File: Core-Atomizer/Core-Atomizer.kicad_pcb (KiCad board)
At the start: 2 copper layers, 23 x 14 mm, 16 parts, among them J1 PH-4AW, J2 PH-2AW环保, Q1 CJ2102, Q2 CJ2102, U1 NL17SZ14DFT2G

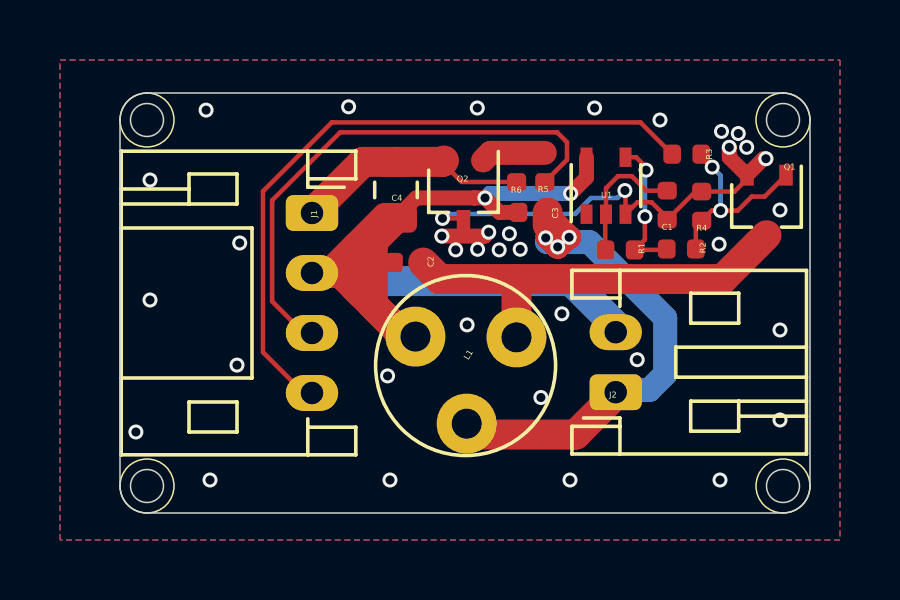
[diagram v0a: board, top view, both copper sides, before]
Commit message: 订正inductor封装，增加丝印
Signed-off-by: fuhua-chen <fuhua-chen@outlook.com>
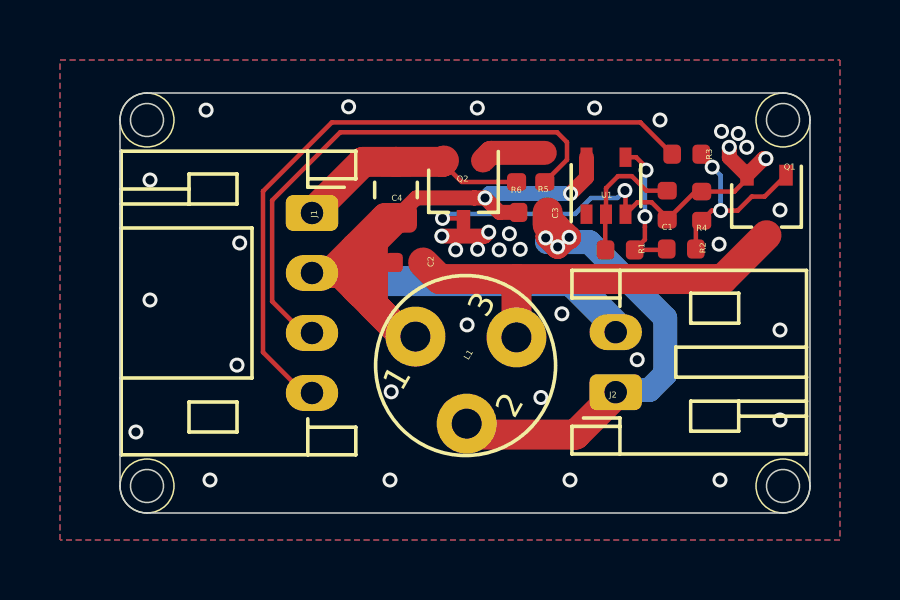
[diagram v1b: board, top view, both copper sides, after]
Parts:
- L1: footprint Inductor_3Pins_6x8mm -> Pinno:Inductor_3Pins_6x8mm
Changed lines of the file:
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@@
   (page A4)
   (layers
-    (0 F.Cu signal hide)
-    (31 B.Cu signal hide)
-    (32 B.Adhes user hide)
-    (33 F.Adhes user hide)
-    (34 B.Paste user hide)
-    (35 F.Paste user hide)
+    (0 F.Cu signal)
+    (31 B.Cu signal)
+    (32 B.Adhes user)
+    (33 F.Adhes user)
+    (34 B.Paste user)
+    (35 F.Paste user)
     (36 B.SilkS user)
     (37 F.SilkS user)
-    (38 B.Mask user hide)
-    (39 F.Mask user hide)
+    (38 B.Mask user)
+    (39 F.Mask user)
     (40 Dwgs.User user)
     (41 Cmts.User user)
@@
   )
   (setup
-    (last_trace_width 0.5)
+    (last_trace_width 0.152)
     (user_trace_width 0.254)
     (user_trace_width 0.5)
@@
     (pad_to_mask_clearance 0)
     (aux_axis_origin 0 0)
-    (visible_elements FFFFFF7F)
+    (visible_elements 7FFFFFFF)
     (pcbplotparams
       (layerselection 0x010fc_ffffffff)
-      (usegerberextensions false)
+      (usegerberextensions true)
       (usegerberattributes false)
       (usegerberadvancedattributes false)
-      (creategerberjobfile false)
+      (creategerberjobfile true)
       (excludeedgelayer true)
-      (linewidth 0.100000)
+      (linewidth 0.020000)
       (plotframeref false)
       (viasonmask false)
@@
       (psnegative false)
       (psa4output false)
-      (plotreference true)
-      (plotvalue true)
+      (plotreference false)
+      (plotvalue false)
       (plotinvisibletext false)
-      (padsonsilk false)
+      (padsonsilk true)
       (subtractmaskfromsilk false)
       (outputformat 1)
       (mirror false)
-      (drillshape 1)
+      (drillshape 0)
       (scaleselection 1)
-      (outputdirectory ""))
+      (outputdirectory "Core-Atomizer v0.1-Gerber"))
   )
   (net 0 "")
@@
     (add_net "Net-(Q2-Pad1)")
     (add_net "Net-(R1-Pad2)")
-    (add_net "Net-(U1-Pad1)")
+  )
+  (module Pinno:Inductor_3Pins_6x8mm (layer F.Cu)
+    (at 123.52 75.184 60)
+    (fp_text reference L1 (at 0.36 -0.1 60) (layer F.SilkS)
+      (effects (font (size 0.2 0.2) (thickness 0.05)))
+    )
+    (fp_text value IND_3Pins_22uH_720uH_6x8mm (at -0.004049 -0.575013 60) (layer F.Fab)
+      (effects (font (size 0.2 0.2) (thickness 0.05)))
+    )
+    (fp_text user 3 (at 2.04 -0.55 60) (layer F.SilkS)
+      (effects (font (size 0.8 0.8) (thickness 0.15)))
+    )
+    (fp_text user 2 (at -0.4 1.93 60) (layer F.SilkS)
+      (effects (font (size 0.8 0.8) (thickness 0.15)))
+    )
+    (fp_text user 1 (at -1.5 -1.77 60) (layer F.SilkS)
+      (effects (font (size 0.8 0.8) (thickness 0.15)))
+    )
+    (fp_text user %R (at 0.36 -0.1 60) (layer F.Fab)
+      (effects (font (size 0.2 0.2) (thickness 0.05)))
+    )
+    (fp_circle (center 0 0) (end 3 0) (layer F.SilkS) (width 0.12))
+    (pad 3 thru_hole circle (at 1.66 1 60) (size 2 2) (drill 1) (layers *.Cu *.Mask)
+      (net 2 "Net-(C2-Pad2)"))
+    (pad 2 thru_hole circle (at -1.66 1 60) (size 2 2) (drill 1) (layers *.Cu *.Mask)
+      (net 4 "Net-(C3-Pad2)"))
+    (pad 1 thru_hole circle (at 0 -1.93 60) (size 2 2) (drill 1) (layers *.Cu *.Mask)
+      (net 3 /VCC))
   )
   (module R_0402_1005Metric (layer F.Cu)
@@
     )
   )
-  (module Inductor_3Pins_6x8mm (layer F.Cu)
-    (at 123.52 75.184 60)
-    (fp_text reference L1 (at 0.36 -0.1 60) (layer F.SilkS)
-      (effects (font (size 0.2 0.2) (thickness 0.05)))
-    )
-    (fp_text value IND_3Pins_22uH_720uH_6x8mm (at -0.004049 -0.575013 60) (layer F.Fab)
-      (effects (font (size 0.2 0.2) (thickness 0.05)))
-    )
-    (fp_circle (center 0 0) (end 3 0) (layer F.SilkS) (width 0.12))
-    (fp_text user %R (at 0.36 -0.1 60) (layer F.Fab)
-      (effects (font (size 0.2 0.2) (thickness 0.05)))
-    )
-    (pad 1 thru_hole circle (at 0 -1.93 60) (size 2 2) (drill 1) (layers *.Cu *.Mask)
-      (net 3 /VCC))
-    (pad 2 thru_hole circle (at -1.66 1 60) (size 2 2) (drill 1) (layers *.Cu *.Mask)
-      (net 4 "Net-(C3-Pad2)"))
-    (pad 3 thru_hole circle (at 1.66 1 60) (size 2 2) (drill 1) (layers *.Cu *.Mask)
-      (net 2 "Net-(C2-Pad2)"))
-  )
   (module SOT-323_SC-70 (layer F.Cu)
     (at 133.55 69.84 270)
@@
   (segment (start 129.542444 69.355) (end 129.059442 68.871998) (width 0.152) (layer F.Cu) (net 1))
   (segment (start 130.24 69.355) (end 129.542444 69.355) (width 0.152) (layer F.Cu) (net 1))
-  (segment (start 131.18 69.385) (end 131.39 69.385) (width 0.152) (layer F.Cu) (net 11))
-  (segment (start 130.24 70.325) (end 131.18 69.385) (width 0.152) (layer F.Cu) (net 11))
-  (segment (start 129.719441 69.741999) (end 129.248001 69.741999) (width 0.152) (layer F.Cu) (net 11))
-  (segment (start 130.24 70.325) (end 130.24 70.262558) (width 0.152) (layer F.Cu) (net 11))
-  (segment (start 130.24 70.262558) (end 129.719441 69.741999) (width 0.152) (layer F.Cu) (net 11))
-  (segment (start 129.248001 69.741999) (end 128.85 70.14) (width 0.152) (layer F.Cu) (net 11))
-  (via (at 128.83 69.35) (size 0.5) (drill 0.3) (layers F.Cu B.Cu) (net 11))
-  (segment (start 128.85 69.37) (end 128.83 69.35) (width 0.152) (layer F.Cu) (net 11))
-  (segment (start 128.85 70.14) (end 128.85 69.37) (width 0.152) (layer F.Cu) (net 11))
-  (segment (start 128.580001 69.599999) (end 127.700001 69.599999) (width 0.152) (layer B.Cu) (net 11))
-  (segment (start 128.83 69.35) (end 128.580001 69.599999) (width 0.152) (layer B.Cu) (net 11))
-  (segment (start 127.700001 69.599999) (end 127.17 70.13) (width 0.152) (layer B.Cu) (net 11))
-  (via (at 122.75 70.28) (size 0.5) (drill 0.3) (layers F.Cu B.Cu) (net 11))
-  (segment (start 127.17 70.13) (end 122.9 70.13) (width 0.152) (layer B.Cu) (net 11))
-  (segment (start 122.9 70.13) (end 122.75 70.28) (width 0.152) (layer B.Cu) (net 11))
-  (segment (start 123.38 70.28) (end 123.45 70.35) (width 0.152) (layer F.Cu) (net 11))
-  (segment (start 122.75 70.28) (end 123.38 70.28) (width 0.152) (layer F.Cu) (net 11))
-  (segment (start 132.9 68.965) (end 132.9 68.84) (width 0.152) (layer F.Cu) (net 11))
-  (segment (start 132.48 69.385) (end 132.9 68.965) (width 0.152) (layer F.Cu) (net 11))
-  (segment (start 131.39 69.385) (end 132.48 69.385) (width 0.152) (layer F.Cu) (net 11))
-  (segment (start 131.36 70.325) (end 131.39 70.355) (width 0.152) (layer F.Cu) (net 8))
   (segment (start 122.105 71.75) (end 122.65701 72.30201) (width 1) (layer F.Cu) (net 2))
   (segment (start 125.216025 72.317995) (end 125.216025 74.612398) (width 1) (layer F.Cu) (net 2))
@@
   (segment (start 116.76599 69.37401) (end 116.76599 74.74099) (width 0.152) (layer F.Cu) (net 7))
   (segment (start 118.125 76.1) (end 118.4 76.1) (width 0.152) (layer F.Cu) (net 7))
+  (segment (start 131.36 70.325) (end 131.39 70.355) (width 0.152) (layer F.Cu) (net 8))
   (segment (start 131.195 70.55) (end 131.39 70.355) (width 0.152) (layer F.Cu) (net 8))
   (segment (start 131.195 71.3) (end 131.195 70.55) (width 0.152) (layer F.Cu) (net 8))
@@
   (segment (start 129.496977 70.988023) (end 129.496977 70.574425) (width 0.152) (layer F.Cu) (net 10))
   (segment (start 129.155 71.33) (end 129.496977 70.988023) (width 0.152) (layer F.Cu) (net 10))
+  (segment (start 131.18 69.385) (end 131.39 69.385) (width 0.152) (layer F.Cu) (net 11))
+  (segment (start 130.24 70.325) (end 131.18 69.385) (width 0.152) (layer F.Cu) (net 11))
+  (segment (start 129.719441 69.741999) (end 129.248001 69.741999) (width 0.152) (layer F.Cu) (net 11))
+  (segment (start 130.24 70.325) (end 130.24 70.262558) (width 0.152) (layer F.Cu) (net 11))
+  (segment (start 130.24 70.262558) (end 129.719441 69.741999) (width 0.152) (layer F.Cu) (net 11))
+  (segment (start 129.248001 69.741999) (end 128.85 70.14) (width 0.152) (layer F.Cu) (net 11))
+  (via (at 128.83 69.35) (size 0.5) (drill 0.3) (layers F.Cu B.Cu) (net 11))
+  (segment (start 128.85 69.37) (end 128.83 69.35) (width 0.152) (layer F.Cu) (net 11))
+  (segment (start 128.85 70.14) (end 128.85 69.37) (width 0.152) (layer F.Cu) (net 11))
+  (segment (start 128.580001 69.599999) (end 127.700001 69.599999) (width 0.152) (layer B.Cu) (net 11))
+  (segment (start 128.83 69.35) (end 128.580001 69.599999) (width 0.152) (layer B.Cu) (net 11))
+  (segment (start 127.700001 69.599999) (end 127.17 70.13) (width 0.152) (layer B.Cu) (net 11))
+  (via (at 122.75 70.28) (size 0.5) (drill 0.3) (layers F.Cu B.Cu) (net 11))
+  (segment (start 127.17 70.13) (end 122.9 70.13) (width 0.152) (layer B.Cu) (net 11))
+  (segment (start 122.9 70.13) (end 122.75 70.28) (width 0.152) (layer B.Cu) (net 11))
+  (segment (start 123.38 70.28) (end 123.45 70.35) (width 0.152) (layer F.Cu) (net 11))
+  (segment (start 122.75 70.28) (end 123.38 70.28) (width 0.152) (layer F.Cu) (net 11))
+  (segment (start 132.9 68.965) (end 132.9 68.84) (width 0.152) (layer F.Cu) (net 11))
+  (segment (start 132.48 69.385) (end 132.9 68.965) (width 0.152) (layer F.Cu) (net 11))
+  (segment (start 131.39 69.385) (end 132.48 69.385) (width 0.152) (layer F.Cu) (net 11))
   (via (at 112.53 77.4) (size 0.5) (drill 0.3) (layers F.Cu B.Cu) (net 11))
   (via (at 113 73) (size 0.5) (drill 0.3) (layers F.Cu B.Cu) (net 11))
@@
   (via (at 115.99 71.1) (size 0.5) (drill 0.3) (layers F.Cu B.Cu) (net 11))
   (via (at 115.9 75.17) (size 0.5) (drill 0.3) (layers F.Cu B.Cu) (net 11))
-  (via (at 120.92 75.53) (size 0.5) (drill 0.3) (layers F.Cu B.Cu) (net 11))
+  (via (at 121.04 76.06) (size 0.5) (drill 0.3) (layers F.Cu B.Cu) (net 11))
   (via (at 123.57 73.83) (size 0.5) (drill 0.3) (layers F.Cu B.Cu) (net 11))
   (via (at 122.73 70.87) (size 0.5) (drill 0.3) (layers F.Cu B.Cu) (net 11))

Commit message: 更改升压电感的错误引脚号，3->2,2->3,并变更PCB
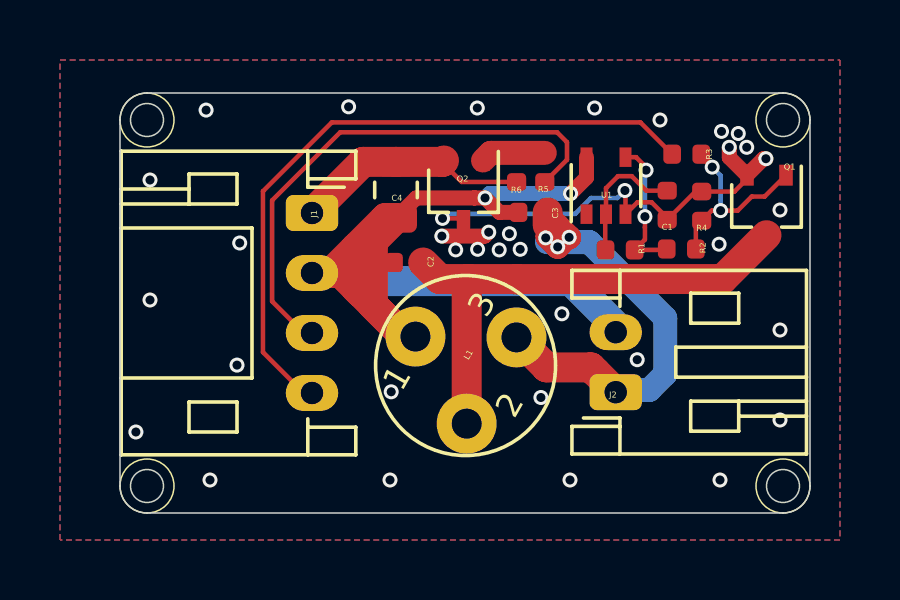
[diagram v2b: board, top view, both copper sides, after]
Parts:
- L1: footprint Pinno:Inductor_3Pins_6x8mm -> Inductor_3Pins_6x8mm
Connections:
- L1 pad 2: Net-(C3-Pad2) -> Net-(C2-Pad2)
- L1 pad 3: Net-(C2-Pad2) -> Net-(C3-Pad2)
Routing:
- net Net-(C2-Pad2): track 14.6 -> 17.1 mm
- net Net-(C3-Pad2): track 18.1 -> 16.5 mm
- net GND: vias 37 -> 36

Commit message: debug震荡电容为2.2nF,震荡频率实测40~50kHz
Signed-off-by: fuhua-chen <fuhua-chen@outlook.com>
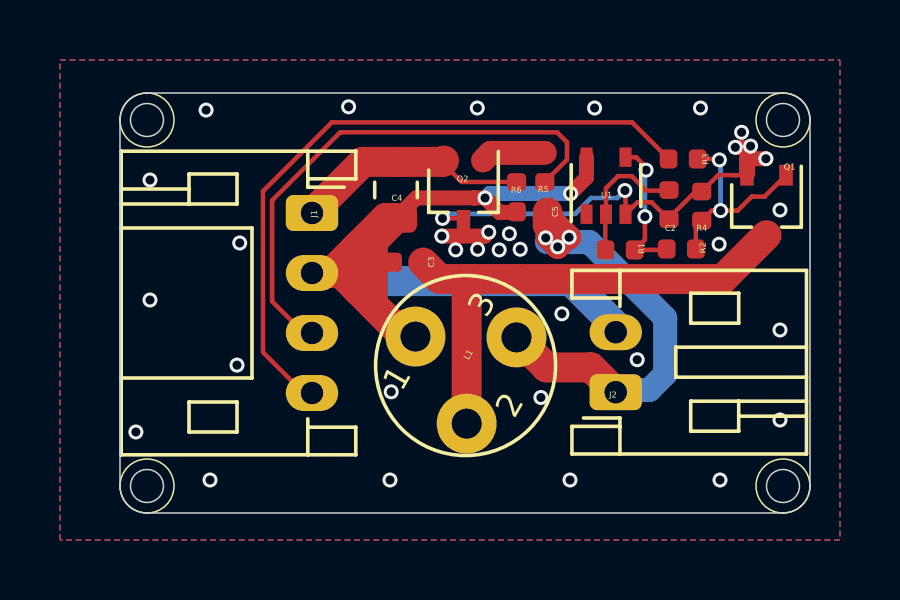
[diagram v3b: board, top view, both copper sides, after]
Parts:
- removed C1: 330pF, C_0402_1005Metric
- added C5: 2.2nF, C_0402_1005Metric, F.Cu at (125.7, 70.1)
- C2, C3: value 330pF -> 2.2nF
- moved C2 8.89 mm to (130.3, 69.8), turned to 270 degrees
- moved C3 4.50 mm to (121.6, 71.7)
- moved R3 0.20 mm to (130.8, 68.3)
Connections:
- C2 pad 1: /VCC -> Net-(C2-Pad1)
- C2 pad 2: Net-(C2-Pad2) -> GND
- J2 pad 1: Net-(C3-Pad2) -> Net-(C5-Pad2)
- L1 pad 2: Net-(C2-Pad2) -> Net-(C3-Pad2)
- L1 pad 3: Net-(C3-Pad2) -> Net-(C5-Pad2)
- Q1 pad 3: Net-(C2-Pad2) -> Net-(C3-Pad2)
- R1 pad 1: Net-(C1-Pad1) -> Net-(C2-Pad1)
- U1 pad 2: Net-(C1-Pad1) -> Net-(C2-Pad1)
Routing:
- net Net-(C2-Pad2): track 17.1 -> 0.00 mm
- net Net-(C5-Pad2): track 0.00 -> 16.5 mm, vias 0 -> 3
- net Net-(C2-Pad1): track 0.00 -> 4.47 mm
- net Net-(C1-Pad1): track 4.40 -> 0.00 mm
- net Net-(C3-Pad2): track 16.5 -> 17.1 mm, vias 3 -> 0
- net GND: track 16.8 -> 17.1 mm, vias 36 -> 35
